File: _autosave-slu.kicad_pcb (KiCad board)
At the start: 2 copper layers, 99.6 x 100.9 mm, 168 parts, among them J1 lcd_out, sw1 sw_2pos

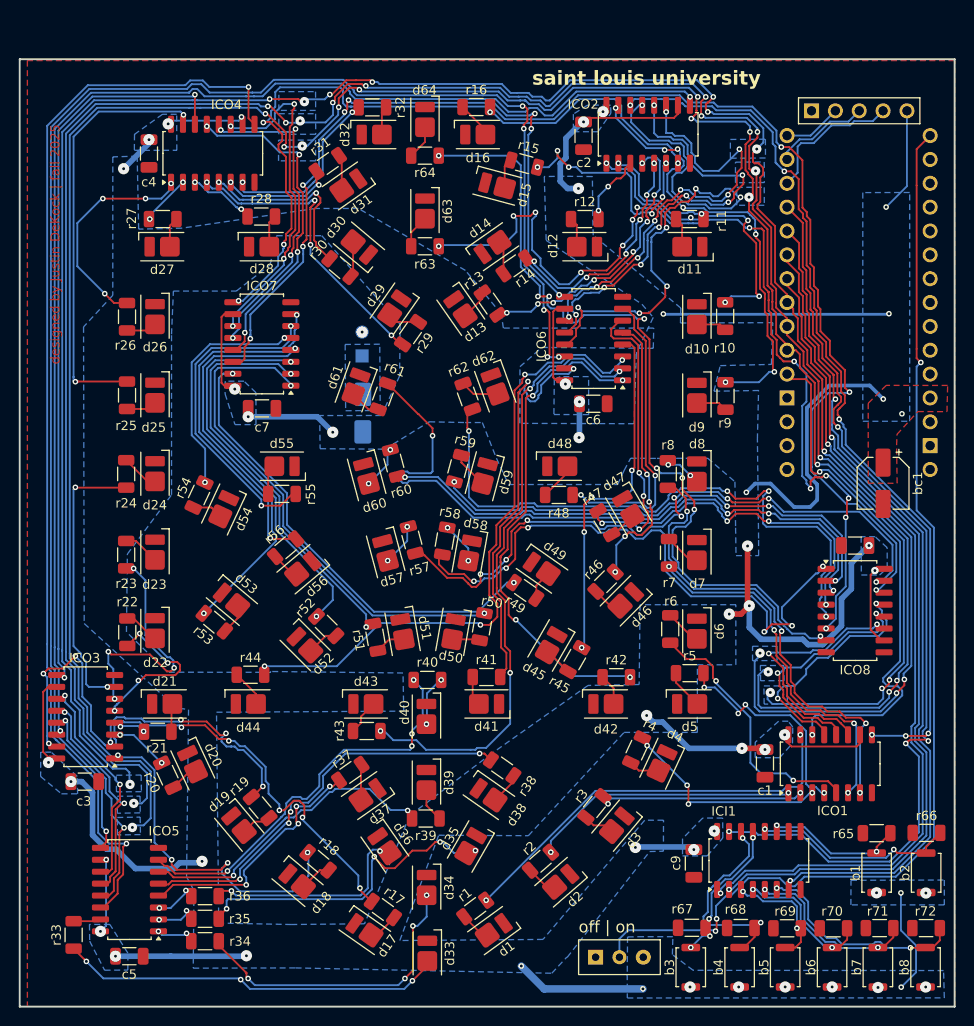
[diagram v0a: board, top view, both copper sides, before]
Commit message: project name engraving added
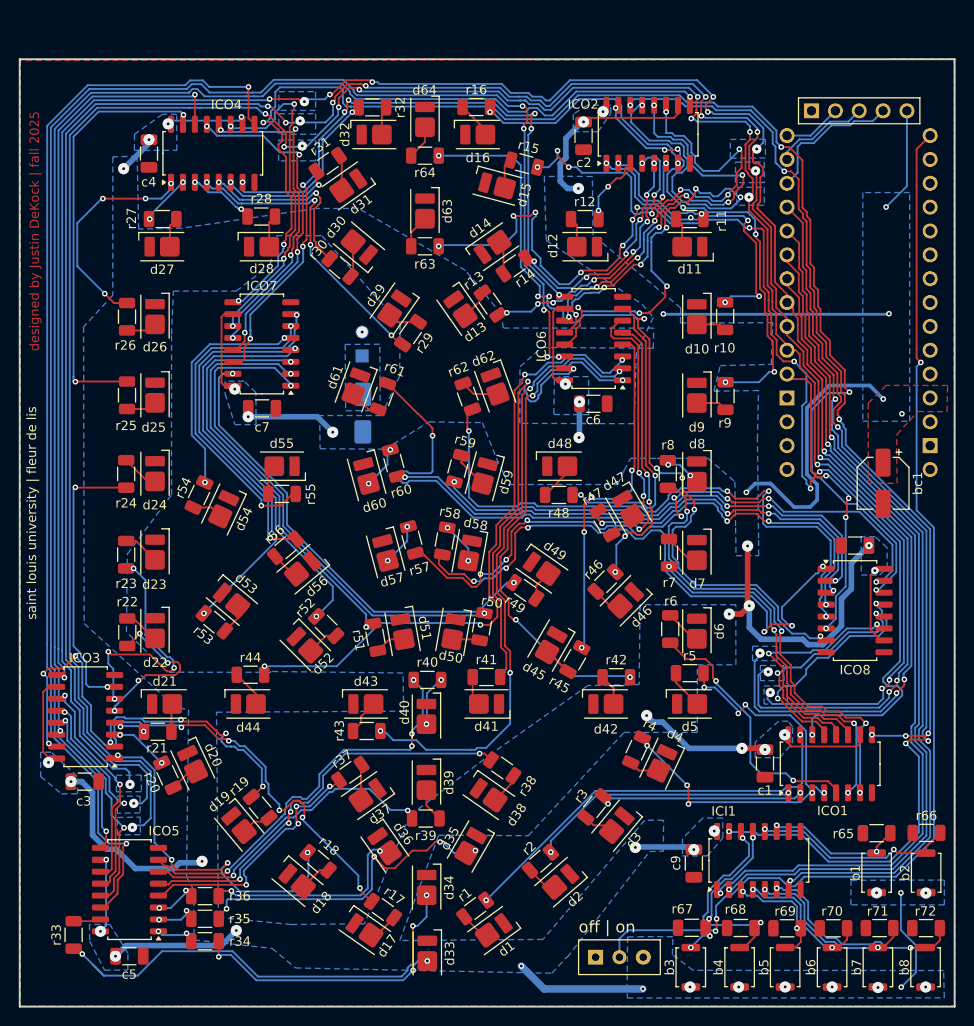
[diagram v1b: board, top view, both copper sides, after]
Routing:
- net Net-(d33-A): track 41.0 -> 43.0 mm, vias 3 -> 2
- net Net-(d34-A): track 34.1 -> 35.0 mm
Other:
- board text added: "saint louis university | fleur de lis"
- board text removed: "saint louis university"
